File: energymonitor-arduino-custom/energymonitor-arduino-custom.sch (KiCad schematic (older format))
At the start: 17 parts

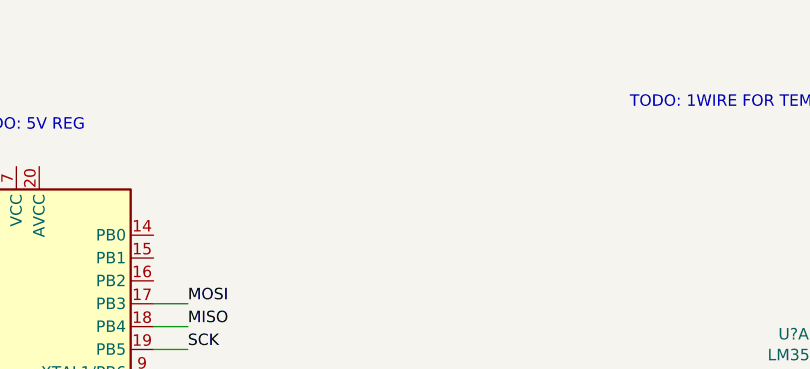
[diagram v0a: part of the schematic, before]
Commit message: Add 3v3 reg
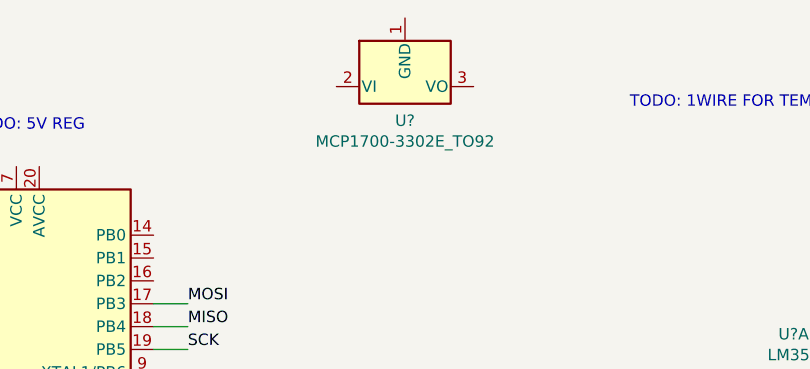
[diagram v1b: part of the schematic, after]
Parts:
- added U?: MCP1700-3302E_TO92, Package_TO_SOT_THT:TO-92_Inline, symbol Regulator_Linear:MCP1700-3302E_TO92
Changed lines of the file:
@@
 Text Notes 6000 1750 2    50   ~ 0
 TODO: 1WIRE FOR TEMPERATURE SENSOR
+$Comp
+L Regulator_Linear:MCP1700-3302E_TO92 U?
+U 1 1 62682D7D
+P 3550 1650
+F 0 "U?" H 3550 1501 50  0000 C CNN
+F 1 "MCP1700-3302E_TO92" H 3550 1410 50  0000 C CNN
+F 2 "Package_TO_SOT_THT:TO-92_Inline" H 3550 1450 50  0001 C CIN
+F 3 "http://ww1.microchip.com/downloads/en/DeviceDoc/20001826D.pdf" H 3550 1650 50  0001 C CNN
+	1    3550 1650
+	1    0    0    -1
+$EndComp
 $EndSCHEMATC

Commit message: Add some pcb layout
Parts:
- added J4: Raspberry_Pi_2_3, symbol Connector:Raspberry_Pi_2_3
- gave numbers to parts that had none: 16
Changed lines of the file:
@@
 $EndDescr
 $Comp
-L MCU_Microchip_ATmega:ATmega328-PU U?
+L MCU_Microchip_ATmega:ATmega328-PU U1
 U 1 1 626639E5
 P 1850 3500
-F 0 "U?" H 1206 3546 50  0000 R CNN
+F 0 "U1" H 1206 3546 50  0000 R CNN
 F 1 "ATmega328-PU" H 1206 3455 50  0000 R CNN
 F 2 "Package_DIP:DIP-28_W7.62mm" H 1850 3500 50  0001 C CIN
@@
 $EndComp
 $Comp
-L Connector_Generic:Conn_02x03_Odd_Even J?
+L Connector_Generic:Conn_02x03_Odd_Even J8
 U 1 1 6266524A
 P 8900 3200
-F 0 "J?" H 8950 3517 50  0000 C CNN
+F 0 "J8" H 8950 3517 50  0000 C CNN
 F 1 "Conn_02x03_Odd_Even" H 8950 3426 50  0000 C CNN
 F 2 "" H 8900 3200 50  0001 C CNN
@@
 $EndComp
 $Comp
-L Connector:Conn_01x05_Male J?
+L Connector:Conn_01x05_Male J6
 U 1 1 62665D2F
 P 8850 4300
-F 0 "J?" H 8822 4232 50  0000 R CNN
+F 0 "J6" H 8822 4232 50  0000 R CNN
 F 1 "Conn_01x06_Male" H 8822 4323 50  0000 R CNN
 F 2 "" H 8850 4300 50  0001 C CNN
@@
 FTDI
 $Comp
-L Connector:DB9_Female_MountingHoles J?
+L Connector:DB9_Female_MountingHoles J7
 U 1 1 62667C05
 P 8850 5350
-F 0 "J?" H 9030 5352 50  0000 L CNN
+F 0 "J7" H 9030 5352 50  0000 L CNN
 F 1 "DB9_Female_MountingHoles" H 9030 5261 50  0000 L CNN
 F 2 "" H 8850 5350 50  0001 C CNN
@@
 Serial
 $Comp
-L Connector:Barrel_Jack_Switch J?
+L Connector:Barrel_Jack_Switch J1
 U 1 1 62670264
 P 3300 5700
-F 0 "J?" H 3357 6017 50  0000 C CNN
+F 0 "J1" H 3357 6017 50  0000 C CNN
 F 1 "Barrel_Jack_Switch" H 3357 5926 50  0000 C CNN
 F 2 "" H 3350 5660 50  0001 C CNN
@@
 $EndComp
 $Comp
-L Connector:AudioJack3_SwitchTR J?
+L Connector:AudioJack3_SwitchTR J2
 U 1 1 6267128C
 P 3350 6500
-F 0 "J?" H 3332 6825 50  0000 C CNN
+F 0 "J2" H 3332 6825 50  0000 C CNN
 F 1 "AudioJack3_SwitchTR" H 3332 6734 50  0000 C CNN
 F 2 "" H 3350 6500 50  0001 C CNN
@@
 	1850 5000 1850 5200
 $Comp
-L Amplifier_Operational:LM358 U?
+L Amplifier_Operational:LM358 U3
 U 1 1 62674131
 P 5250 3100
-F 0 "U?" H 5250 3467 50  0000 C CNN
+F 0 "U3" H 5250 3467 50  0000 C CNN
 F 1 "LM358" H 5250 3376 50  0000 C CNN
 F 2 "" H 5250 3100 50  0001 C CNN
@@
 $EndComp
 $Comp
-L Amplifier_Operational:LM358 U?
+L Amplifier_Operational:LM358 U3
 U 2 1 62674F47
 P 6900 5900
-F 0 "U?" H 6900 6267 50  0000 C CNN
+F 0 "U3" H 6900 6267 50  0000 C CNN
 F 1 "LM358" H 6900 6176 50  0000 C CNN
 F 2 "" H 6900 5900 50  0001 C CNN
@@
 $EndComp
 $Comp
-L Amplifier_Operational:LM358 U?
+L Amplifier_Operational:LM358 U3
 U 3 1 6267642A
 P 6050 5950
-F 0 "U?" H 6008 5996 50  0000 L CNN
+F 0 "U3" H 6008 5996 50  0000 L CNN
 F 1 "LM358" H 6008 5905 50  0000 L CNN
 F 2 "" H 6050 5950 50  0001 C CNN
@@
 	4700 3000 4950 3000
 $Comp
-L Device:R R?
+L Device:R R4
 U 1 1 626A0012
 P 4650 4150
-F 0 "R?" H 4720 4196 50  0000 L CNN
+F 0 "R4" H 4720 4196 50  0000 L CNN
 F 1 "R" H 4720 4105 50  0000 L CNN
 F 2 "" V 4580 4150 50  0001 C CNN
@@
 $EndComp
 $Comp
-L Device:R R?
+L Device:R R5
 U 1 1 626A098F
 P 4650 4650
-F 0 "R?" H 4720 4696 50  0000 L CNN
+F 0 "R5" H 4720 4696 50  0000 L CNN
 F 1 "R" H 4720 4605 50  0000 L CNN
 F 2 "" V 4580 4650 50  0001 C CNN
@@
 	4650 4400 4650 4300
 $Comp
-L Device:R R?
+L Device:R R3
 U 1 1 626A896A
 P 4100 6550
-F 0 "R?" H 4170 6596 50  0000 L CNN
+F 0 "R3" H 4170 6596 50  0000 L CNN
 F 1 "R" H 4170 6505 50  0000 L CNN
 F 2 "" V 4030 6550 50  0001 C CNN
@@
 	2700 3500 2450 3500
 $Comp
-L Device:R R?
+L Device:R R1
 U 1 1 626AFB1C
 P 3900 5600
-F 0 "R?" V 3693 5600 50  0000 C CNN
+F 0 "R1" V 3693 5600 50  0000 C CNN
 F 1 "R" V 3784 5600 50  0000 C CNN
 F 2 "" V 3830 5600 50  0001 C CNN
@@
 $EndComp
 $Comp
-L Device:R R?
+L Device:R R2
 U 1 1 626B04A8
 P 3900 5800
-F 0 "R?" V 3693 5800 50  0000 C CNN
+F 0 "R2" V 3693 5800 50  0000 C CNN
 F 1 "R" V 3784 5800 50  0000 C CNN
 F 2 "" V 3830 5800 50  0001 C CNN
@@
 I2C LCD
 $Comp
-L Connector:Conn_01x04_Male J?
+L Connector:Conn_01x04_Male J5
 U 1 1 626C3FC6
 P 8850 2150
-F 0 "J?" H 8822 2032 50  0000 R CNN
+F 0 "J5" H 8822 2032 50  0000 R CNN
 F 1 "Conn_01x04_Male" H 8822 2123 50  0000 R CNN
 F 2 "" H 8850 2150 50  0001 C CNN
@@
 	8650 4100 8450 4100
 $Comp
-L Connector:Conn_01x02_Male J?
+L Connector:Conn_01x02_Male J3
 U 1 1 626D596B
 P 6350 4450
-F 0 "J?" H 6458 4631 50  0000 C CNN
+F 0 "J3" H 6458 4631 50  0000 C CNN
 F 1 "Conn_01x02_Male" H 6458 4540 50  0000 C CNN
 F 2 "" H 6350 4450 50  0001 C CNN
@@
 	4100 6800 4100 6950
 $Comp
-L Device:CP C?
+L Device:CP C1
 U 1 1 626FEB22
 P 5100 4700
-F 0 "C?" H 5218 4746 50  0000 L CNN
+F 0 "C1" H 5218 4746 50  0000 L CNN
 F 1 "CP" H 5218 4655 50  0000 L CNN
 F 2 "" H 5138 4550 50  0001 C CNN
@@
 DTR
 $Comp
-L power:GND #PWR?
+L power:GND #PWR0113
 U 1 1 62739103
 P 8300 5950
-F 0 "#PWR?" H 8300 5700 50  0001 C CNN
+F 0 "#PWR0113" H 8300 5700 50  0001 C CNN
 F 1 "GND" H 8305 5777 50  0000 C CNN
 F 2 "" H 8300 5950 50  0001 C CNN
@@
 TODO: 1WIRE FOR TEMPERATURE SENSOR
 $Comp
-L Regulator_Linear:MCP1700-3302E_TO92 U?
+L Regulator_Linear:MCP1700-3302E_TO92 U2
 U 1 1 62682D7D
 P 3550 1650
-F 0 "U?" H 3550 1501 50  0000 C CNN
+F 0 "U2" H 3550 1501 50  0000 C CNN
 F 1 "MCP1700-3302E_TO92" H 3550 1410 50  0000 C CNN
 F 2 "Package_TO_SOT_THT:TO-92_Inline" H 3550 1450 50  0001 C CIN
@@
 	1    0    0    -1
 $EndComp
+$Comp
+L Connector:Raspberry_Pi_2_3 J4
+U 1 1 626A86DC
+P 7050 1950
+F 0 "J4" H 7050 3431 50  0000 C CNN
+F 1 "Raspberry_Pi_2_3" H 7050 3340 50  0000 C CNN
+F 2 "" H 7050 1950 50  0001 C CNN
+F 3 "https://www.raspberrypi.org/documentation/hardware/raspberrypi/schematics/rpi_SCH_3bplus_1p0_reduced.pdf" H 7050 1950 50  0001 C CNN
+	1    7050 1950
+	1    0    0    -1
+$EndComp
